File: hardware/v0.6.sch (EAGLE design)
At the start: 31 parts, among them J2 MAGJACK, U1 ATMEGA168P, U2 ENC28J60, Y1 CRYSTAL-GROUNDED

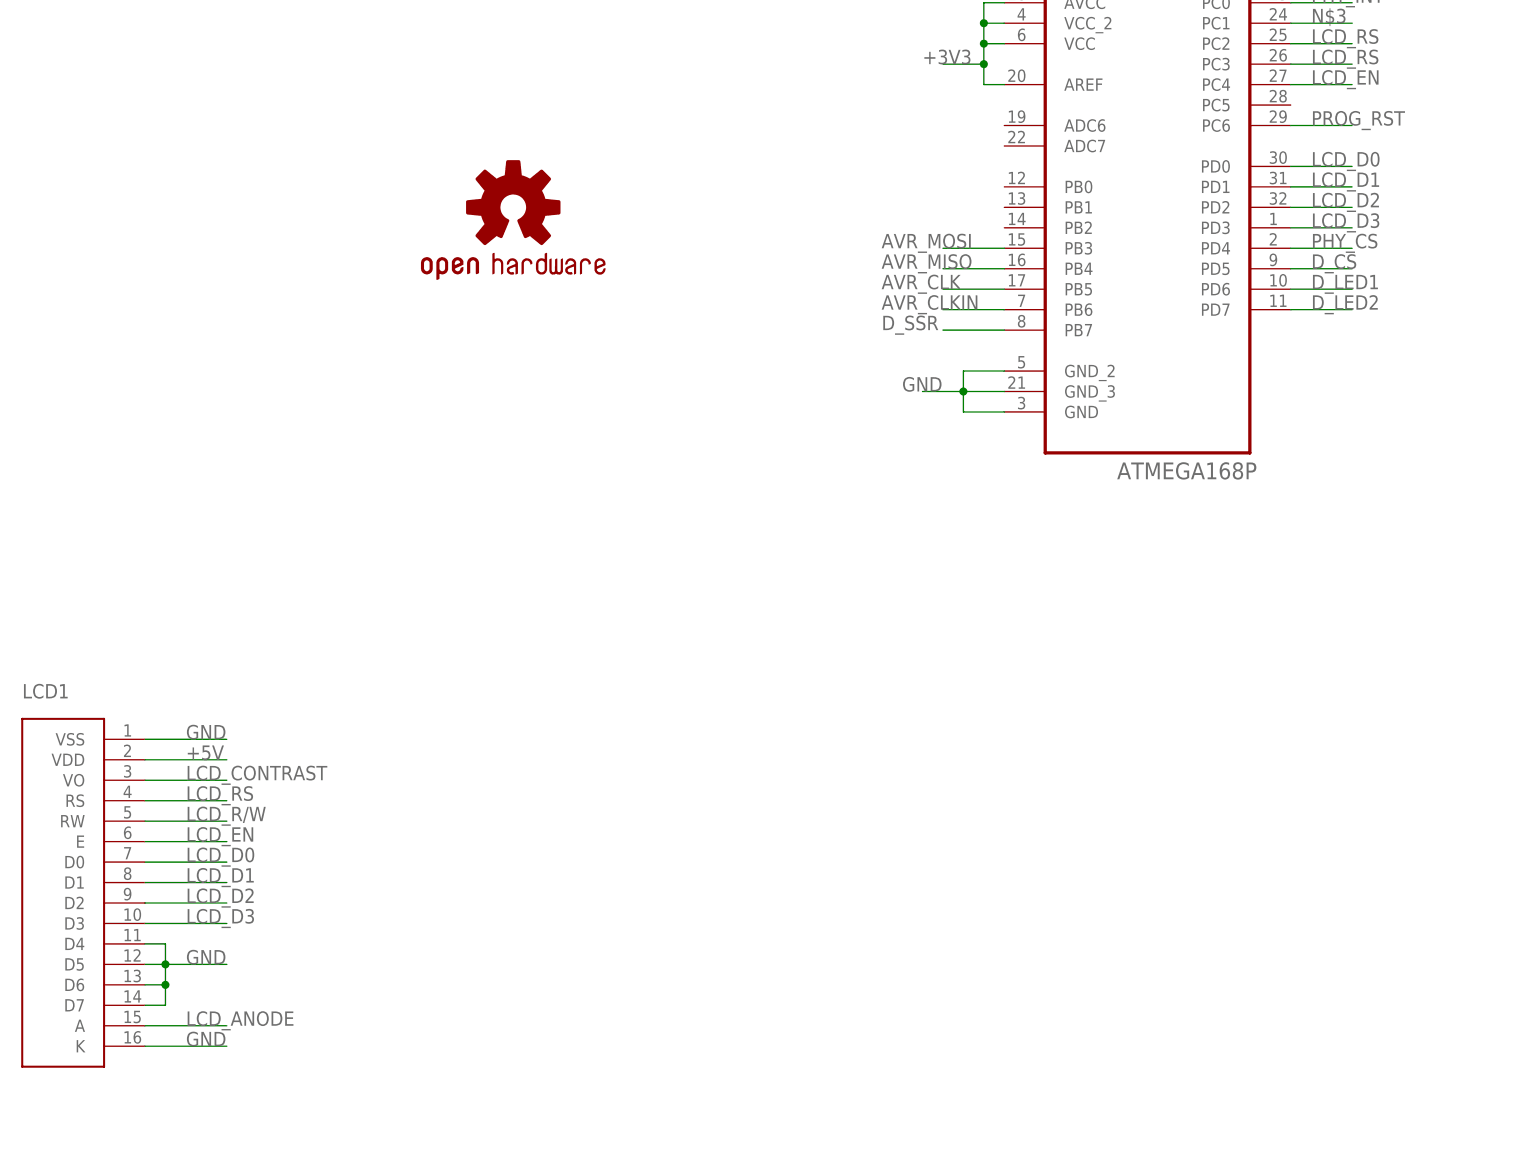
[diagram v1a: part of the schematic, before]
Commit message: routed correct (upper) 4 bit lcd bus (hardware)
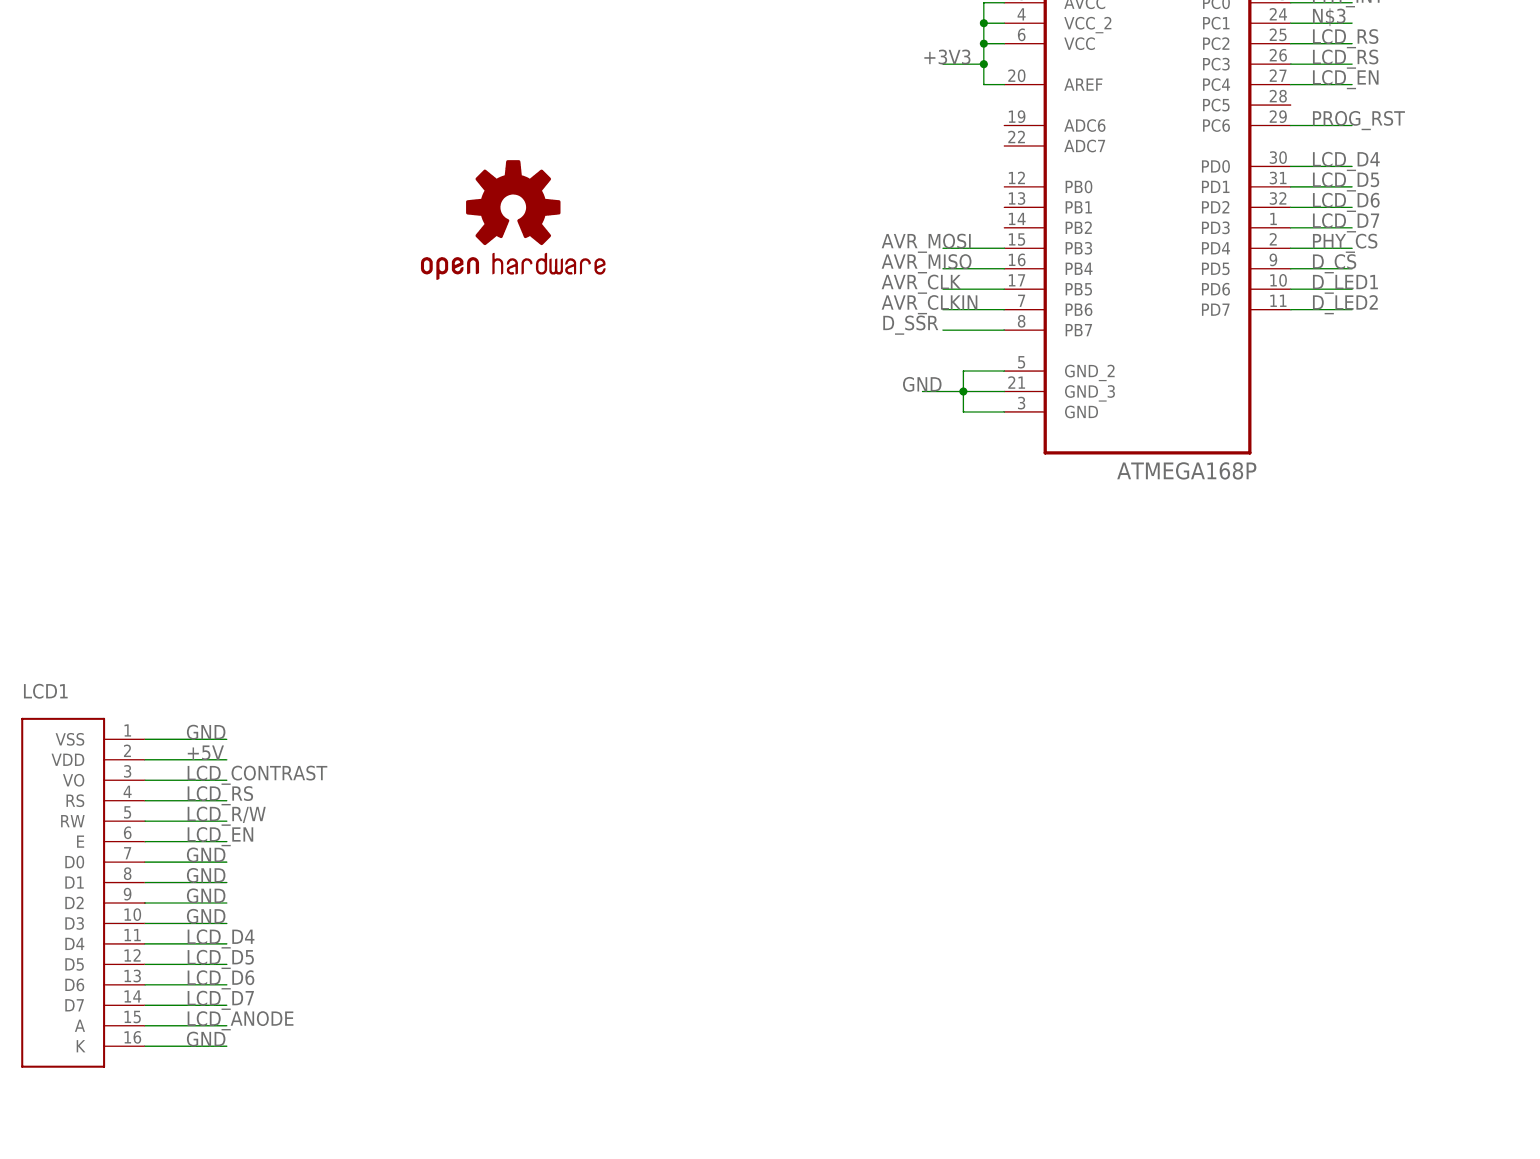
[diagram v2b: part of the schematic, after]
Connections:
- removed net LCD_D0: LCD1.D0, U1.PD0
- removed net LCD_D1: LCD1.D1, U1.PD1
- removed net LCD_D2: LCD1.D2, U1.PD2
- removed net LCD_D3: LCD1.D3, U1.PD3
- new net LCD_D4: LCD1.D4, U1.PD0
- new net LCD_D5: LCD1.D5, U1.PD1
- new net LCD_D6: LCD1.D6, U1.PD2
- new net LCD_D7: LCD1.D7, U1.PD3
- net GND: now also LCD1.D0, LCD1.D1, LCD1.D2, LCD1.D3; no longer LCD1.D4, LCD1.D5, LCD1.D6, LCD1.D7
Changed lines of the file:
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@@
-</segment>
-<segment>
-<pinref part="LCD1" gate="G$1" pin="D4"/>
-<wire x1="-104.14" y1="-177.8" x2="-101.6" y2="-177.8" width="0.1524" layer="91"/>
-<wire x1="-101.6" y1="-177.8" x2="-101.6" y2="-180.34" width="0.1524" layer="91"/>
-<pinref part="LCD1" gate="G$1" pin="D5"/>
-<wire x1="-101.6" y1="-180.34" x2="-104.14" y2="-180.34" width="0.1524" layer="91"/>
-<wire x1="-101.6" y1="-180.34" x2="-101.6" y2="-182.88" width="0.1524" layer="91"/>
-<junction x="-101.6" y="-180.34"/>
-<pinref part="LCD1" gate="G$1" pin="D6"/>
-<wire x1="-101.6" y1="-182.88" x2="-104.14" y2="-182.88" width="0.1524" layer="91"/>
-<wire x1="-101.6" y1="-182.88" x2="-101.6" y2="-185.42" width="0.1524" layer="91"/>
-<junction x="-101.6" y="-182.88"/>
-<pinref part="LCD1" gate="G$1" pin="D7"/>
-<wire x1="-101.6" y1="-185.42" x2="-104.14" y2="-185.42" width="0.1524" layer="91"/>
-<wire x1="-101.6" y1="-180.34" x2="-93.98" y2="-180.34" width="0.1524" layer="91"/>
-<label x="-99.06" y="-180.34" size="1.778" layer="95"/>
 </segment>
 <segment>
@@
 <label x="119.38" y="25.4" size="1.778" layer="95"/>
 </segment>
+<segment>
+<pinref part="LCD1" gate="G$1" pin="D0"/>
+<wire x1="-104.14" y1="-167.64" x2="-93.98" y2="-167.64" width="0.1524" layer="91"/>
+<label x="-99.06" y="-167.64" size="1.778" layer="95"/>
+</segment>
+<segment>
+<pinref part="LCD1" gate="G$1" pin="D1"/>
+<wire x1="-104.14" y1="-170.18" x2="-93.98" y2="-170.18" width="0.1524" layer="91"/>
+<label x="-99.06" y="-170.18" size="1.778" layer="95"/>
+</segment>
+<segment>
+<pinref part="LCD1" gate="G$1" pin="D2"/>
+<wire x1="-104.14" y1="-172.72" x2="-93.98" y2="-172.72" width="0.1524" layer="91"/>
+<label x="-99.06" y="-172.72" size="1.778" layer="95"/>
+</segment>
+<segment>
+<pinref part="LCD1" gate="G$1" pin="D3"/>
+<wire x1="-104.14" y1="-175.26" x2="-93.98" y2="-175.26" width="0.1524" layer="91"/>
+<label x="-99.06" y="-175.26" size="1.778" layer="95"/>
+</segment>
 </net>
 <net name="+5V" class="0">
@@
 <wire x1="38.1" y1="-71.12" x2="45.72" y2="-71.12" width="0.1524" layer="91"/>
 <label x="40.64" y="-71.12" size="1.778" layer="95"/>
-</segment>
-</net>
-<net name="LCD_D0" class="0">
-<segment>
-<pinref part="LCD1" gate="G$1" pin="D0"/>
-<wire x1="-104.14" y1="-167.64" x2="-93.98" y2="-167.64" width="0.1524" layer="91"/>
-<label x="-99.06" y="-167.64" size="1.778" layer="95"/>
-</segment>
-<segment>
-<pinref part="U1" gate="A" pin="PD0"/>
-<wire x1="38.1" y1="-81.28" x2="45.72" y2="-81.28" width="0.1524" layer="91"/>
-<label x="40.64" y="-81.28" size="1.778" layer="95"/>
-</segment>
-</net>
-<net name="LCD_D1" class="0">
-<segment>
-<pinref part="LCD1" gate="G$1" pin="D1"/>
-<wire x1="-104.14" y1="-170.18" x2="-93.98" y2="-170.18" width="0.1524" layer="91"/>
-<label x="-99.06" y="-170.18" size="1.778" layer="95"/>
-</segment>
-<segment>
-<pinref part="U1" gate="A" pin="PD1"/>
-<wire x1="38.1" y1="-83.82" x2="45.72" y2="-83.82" width="0.1524" layer="91"/>
-<label x="40.64" y="-83.82" size="1.778" layer="95"/>
-</segment>
-</net>
-<net name="LCD_D2" class="0">
-<segment>
-<pinref part="LCD1" gate="G$1" pin="D2"/>
-<wire x1="-104.14" y1="-172.72" x2="-93.98" y2="-172.72" width="0.1524" layer="91"/>
-<label x="-99.06" y="-172.72" size="1.778" layer="95"/>
-</segment>
-<segment>
-<pinref part="U1" gate="A" pin="PD2"/>
-<wire x1="38.1" y1="-86.36" x2="45.72" y2="-86.36" width="0.1524" layer="91"/>
-<label x="40.64" y="-86.36" size="1.778" layer="95"/>
-</segment>
-</net>
-<net name="LCD_D3" class="0">
-<segment>
-<pinref part="LCD1" gate="G$1" pin="D3"/>
-<wire x1="-104.14" y1="-175.26" x2="-93.98" y2="-175.26" width="0.1524" layer="91"/>
-<label x="-99.06" y="-175.26" size="1.778" layer="95"/>
-</segment>
-<segment>
-<pinref part="U1" gate="A" pin="PD3"/>
-<wire x1="38.1" y1="-88.9" x2="45.72" y2="-88.9" width="0.1524" layer="91"/>
-<label x="40.64" y="-88.9" size="1.778" layer="95"/>
 </segment>
 </net>
@@
 </segment>
 </net>
+<net name="LCD_D4" class="0">
+<segment>
+<pinref part="U1" gate="A" pin="PD0"/>
+<wire x1="38.1" y1="-81.28" x2="45.72" y2="-81.28" width="0.1524" layer="91"/>
+<label x="40.64" y="-81.28" size="1.778" layer="95"/>
+</segment>
+<segment>
+<pinref part="LCD1" gate="G$1" pin="D4"/>
+<wire x1="-104.14" y1="-177.8" x2="-93.98" y2="-177.8" width="0.1524" layer="91"/>
+<label x="-99.06" y="-177.8" size="1.778" layer="95"/>
+</segment>
+</net>
+<net name="LCD_D5" class="0">
+<segment>
+<pinref part="U1" gate="A" pin="PD1"/>
+<wire x1="38.1" y1="-83.82" x2="45.72" y2="-83.82" width="0.1524" layer="91"/>
+<label x="40.64" y="-83.82" size="1.778" layer="95"/>
+</segment>
+<segment>
+<pinref part="LCD1" gate="G$1" pin="D5"/>
+<wire x1="-93.98" y1="-180.34" x2="-104.14" y2="-180.34" width="0.1524" layer="91"/>
+<label x="-99.06" y="-180.34" size="1.778" layer="95"/>
+</segment>
+</net>
+<net name="LCD_D6" class="0">
+<segment>
+<pinref part="U1" gate="A" pin="PD2"/>
+<wire x1="38.1" y1="-86.36" x2="45.72" y2="-86.36" width="0.1524" layer="91"/>
+<label x="40.64" y="-86.36" size="1.778" layer="95"/>
+</segment>
+<segment>
+<pinref part="LCD1" gate="G$1" pin="D6"/>
+<wire x1="-104.14" y1="-182.88" x2="-93.98" y2="-182.88" width="0.1524" layer="91"/>
+<label x="-99.06" y="-182.88" size="1.778" layer="95"/>
+</segment>
+</net>
+<net name="LCD_D7" class="0">
+<segment>
+<pinref part="U1" gate="A" pin="PD3"/>
+<wire x1="38.1" y1="-88.9" x2="45.72" y2="-88.9" width="0.1524" layer="91"/>
+<label x="40.64" y="-88.9" size="1.778" layer="95"/>
+</segment>
+<segment>
+<pinref part="LCD1" gate="G$1" pin="D7"/>
+<wire x1="-93.98" y1="-185.42" x2="-104.14" y2="-185.42" width="0.1524" layer="91"/>
+<label x="-99.06" y="-185.42" size="1.778" layer="95"/>
+</segment>
+</net>
